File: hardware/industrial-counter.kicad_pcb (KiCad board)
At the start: 2 copper layers, 40 x 40 mm, 45 parts, among them J1 DEBUG, P1 CON-SENSOR2, P2 BOOT, P3 CONN_8, U1 XMC1404, U2 TLP2367, U3 TLP2367, U4 TLP2367, U5 TLP2367, U6 DRILL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

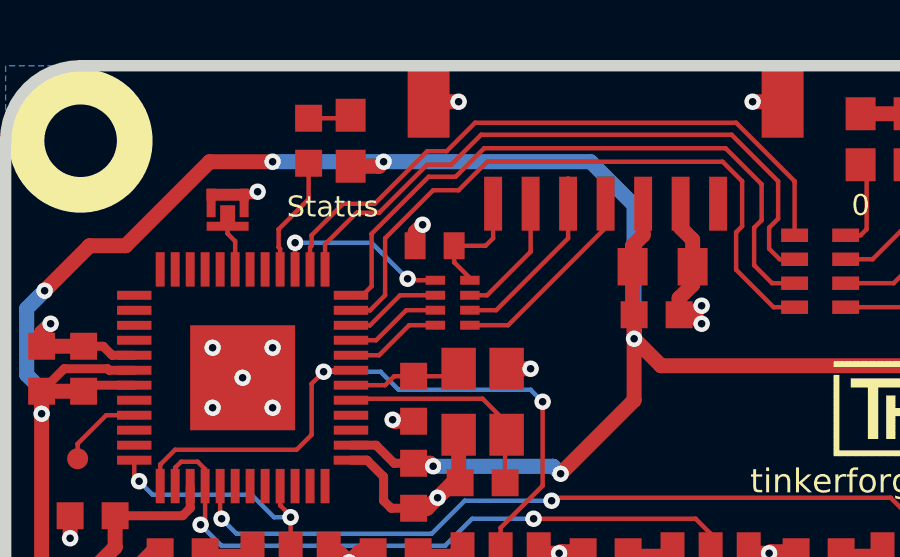
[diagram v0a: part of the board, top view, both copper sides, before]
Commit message: Change capacitor footprint(s) to C0402F
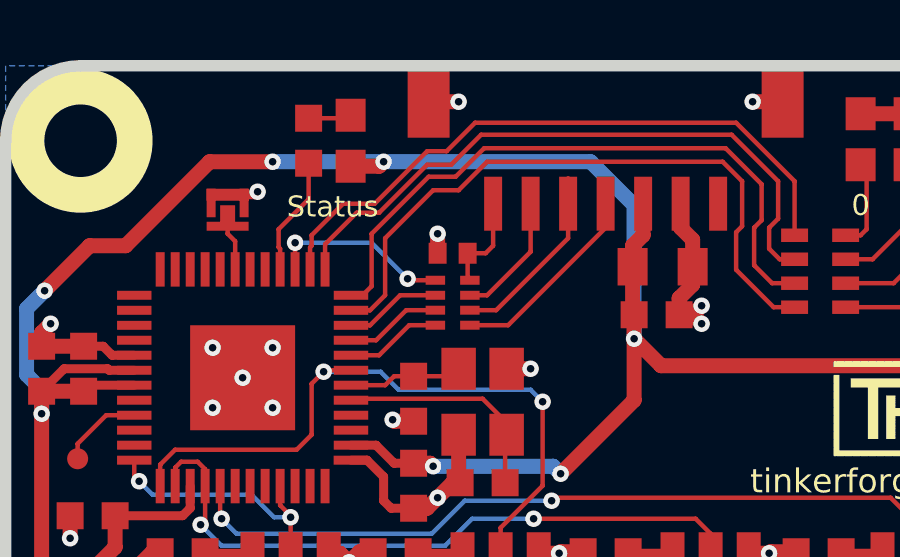
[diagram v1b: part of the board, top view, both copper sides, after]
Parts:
- C1: footprint C0402E -> kicad-libraries:C0402F
- C10, C11, C12, C13, C3, C4, C5, C6, C7, C8, C9: footprint C0603F -> kicad-libraries:C0603F
- C2: footprint C0805 -> kicad-libraries:C0805
- D1, D2, D3, D4, D5: footprint D0603E -> kicad-libraries:D0603E
- P1: footprint CON-SENSOR2 -> kicad-libraries:CON-SENSOR2
- P3: footprint OQ_8P -> kicad-libraries:OQ_8P
- R1: footprint R0603F -> kicad-libraries:R0603F
- R2, R3, R4, R5: footprint R1210 -> kicad-libraries:R1210
- RP1: footprint 4X0402 -> kicad-libraries:4X0402
- moved C1 0.65 mm to (112.7, 44.3)
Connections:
- P1 pad 1: (no net) -> Net-(P1-Pad1)
- U1 pad 10: (no net) -> Net-(U1-Pad10)
- U1 pad 11: (no net) -> Net-(U1-Pad11)
- U1 pad 12: (no net) -> Net-(U1-Pad12)
- U1 pad 13: (no net) -> Net-(U1-Pad13)
- U1 pad 14: (no net) -> Net-(U1-Pad14)
- U1 pad 15: (no net) -> Net-(U1-Pad15)
- U1 pad 16: (no net) -> Net-(U1-Pad16)
- U1 pad 20: (no net) -> Net-(U1-Pad20)
- U1 pad 22: (no net) -> Net-(U1-Pad22)
- U1 pad 23: (no net) -> Net-(U1-Pad23)
- U1 pad 30: (no net) -> Net-(U1-Pad30)
- U1 pad 31: (no net) -> Net-(U1-Pad31)
- U1 pad 32: (no net) -> Net-(U1-Pad32)
- U1 pad 34: (no net) -> Net-(U1-Pad34)
- U1 pad 35: (no net) -> Net-(U1-Pad35)
- U1 pad 36: (no net) -> Net-(U1-Pad36)
- U1 pad 39: (no net) -> Net-(U1-Pad39)
- U1 pad 40: (no net) -> Net-(U1-Pad40)
- U1 pad 5: (no net) -> Net-(U1-Pad5)
- U1 pad 6: (no net) -> Net-(U1-Pad6)
- U1 pad 8: (no net) -> Net-(U1-Pad8)
- U1 pad 9: (no net) -> Net-(U1-Pad9)
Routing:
- net Net-(C1-Pad1): track 3.92 -> 3.36 mm
